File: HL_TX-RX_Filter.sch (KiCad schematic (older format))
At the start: 201 parts, among them J1 CNR1, J10 To Rx in, J2 CNR3, J3 Antenna, J4 CNR2, J5 CNR4, J6 From Tx, J7 ICSP, J8 SCL SDA, J9 Input1, Q1 2N7002, Q2 2N7002, Q3 2N7002, Q4 2N7002, Q5 2N7002, Q6 2N7002, Q7 2N7002, Q8 2N7002, U1 ATMEGA328-AU, U10 PE4259, U11 PE4259, U12 PE4259, U2 PE4259, U3 PE4259, U4 PE4259, U5 PE4259, U6 PE4259, U7 PE4259, U8 PE4259, U9 PE4259

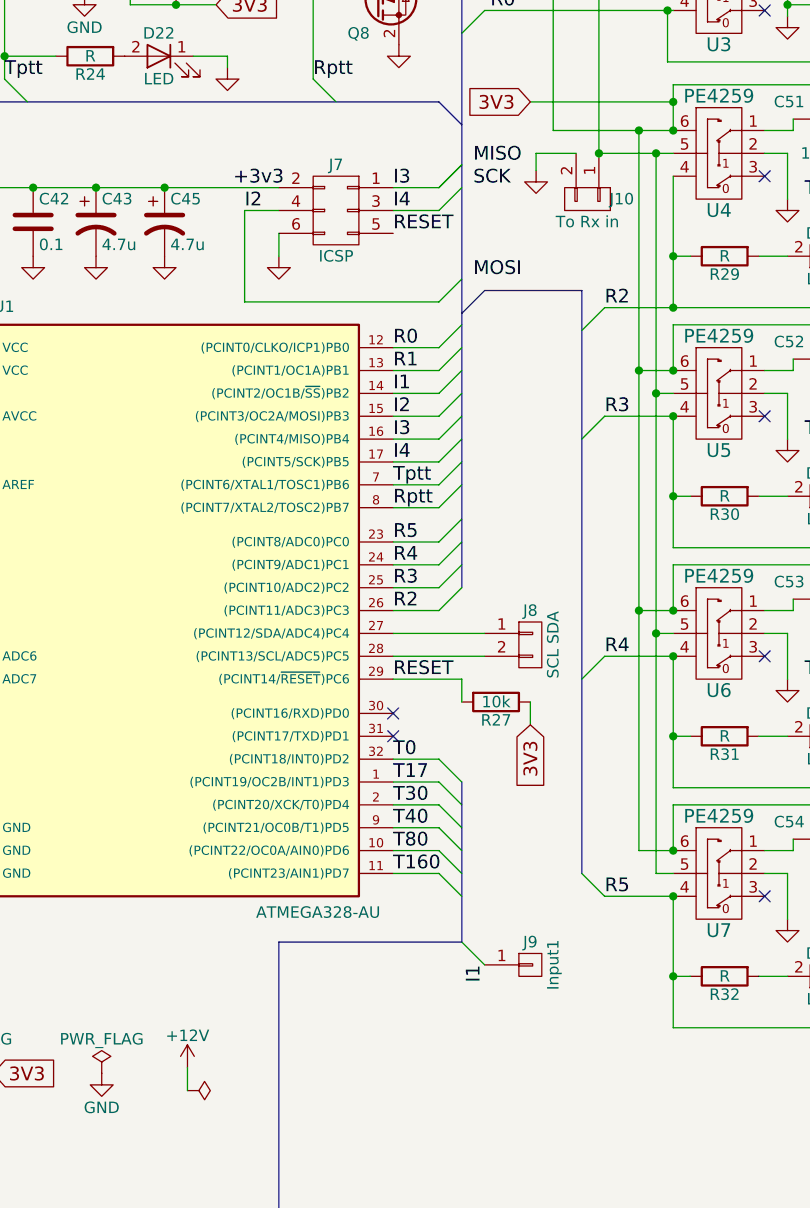
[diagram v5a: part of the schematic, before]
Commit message: Further progress on Filter switching lines
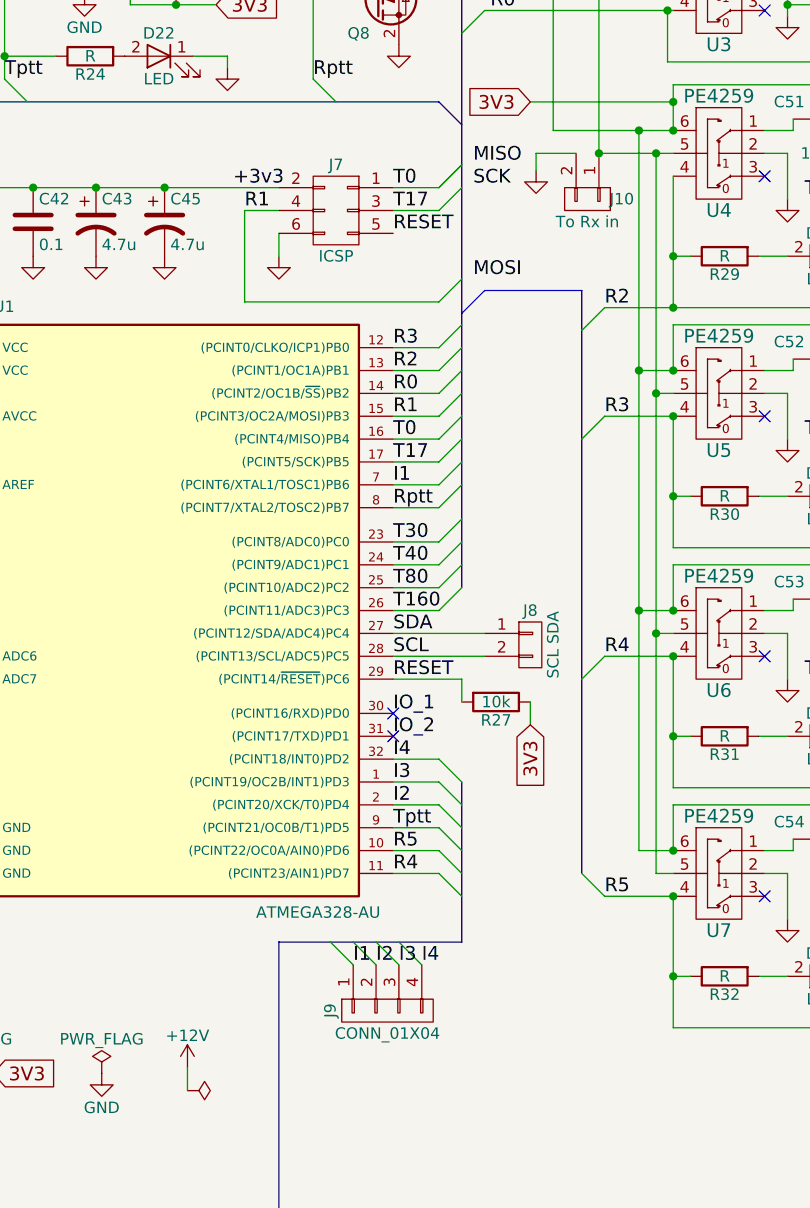
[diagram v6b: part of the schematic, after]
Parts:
- removed J9: Input1, Pin_Headers:Pin_Header_Straight_1x01_Pitch2.54mm, symbol CONN_01X01
- added J9: CONN_01X04, Pin_Headers:Pin_Header_Straight_1x04_Pitch2.54mm, symbol CONN_01X04
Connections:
- net I1: now also U1.7 ((PCINT6/XTAL1/TOSC1)PB6), J9.1 (P1); no longer U1.14 ((PCINT2/OC1B/~SS~)PB2)
- net I2: now also U1.2 ((PCINT20/XCK/T0)PD4), J9.2 (P2); no longer J7.4 (P4), U1.15 ((PCINT3/OC2A/MOSI)PB3)
- net I3: now also U1.1 ((PCINT19/OC2B/INT1)PD3), J9.3 (P3); no longer J7.1 (P1), U1.16 ((PCINT4/MISO)PB4)
- net I4: now also U1.32 ((PCINT18/INT0)PD2), J9.4 (P4); no longer J7.3 (P3), U1.17 ((PCINT5/SCK)PB5)
- net R0: now also U1.14 ((PCINT2/OC1B/~SS~)PB2); no longer U1.12 ((PCINT0/CLKO/ICP1)PB0)
- net R1: now also J7.4 (P4), U1.15 ((PCINT3/OC2A/MOSI)PB3); no longer U1.13 ((PCINT1/OC1A)PB1)
- net R2: now also U1.13 ((PCINT1/OC1A)PB1); no longer U1.26 ((PCINT11/ADC3)PC3)
- net R3: now also U1.12 ((PCINT0/CLKO/ICP1)PB0); no longer U1.25 ((PCINT10/ADC2)PC2)
- net R4: now also U1.11 ((PCINT23/AIN1)PD7); no longer U1.24 ((PCINT9/ADC1)PC1)
- net R5: now also U1.10 ((PCINT22/OC0A/AIN0)PD6); no longer U1.23 ((PCINT8/ADC0)PC0)
- net T0: now also J7.1 (P1), U1.16 ((PCINT4/MISO)PB4); no longer U1.32 ((PCINT18/INT0)PD2)
- net T160: now also U1.26 ((PCINT11/ADC3)PC3); no longer U1.11 ((PCINT23/AIN1)PD7)
- net T17: now also J7.3 (P3), U1.17 ((PCINT5/SCK)PB5); no longer U1.1 ((PCINT19/OC2B/INT1)PD3)
- net T30: now also U1.23 ((PCINT8/ADC0)PC0); no longer U1.2 ((PCINT20/XCK/T0)PD4)
- net T40: now also U1.24 ((PCINT9/ADC1)PC1); no longer U1.9 ((PCINT21/OC0B/T1)PD5)
- net T80: now also U1.25 ((PCINT10/ADC2)PC2); no longer U1.10 ((PCINT22/OC0A/AIN0)PD6)
- net Tptt: now also U1.9 ((PCINT21/OC0B/T1)PD5); no longer U1.7 ((PCINT6/XTAL1/TOSC1)PB6)
- net SDA: now reaches J8.1 (P1), U1.27 ((PCINT12/SDA/ADC4)PC4)
- net SCL: now reaches J8.2 (P2), U1.28 ((PCINT13/SCL/ADC5)PC5)
- net IO_1: now reaches U1.30 ((PCINT16/RXD)PD0)
- net IO_2: now reaches U1.31 ((PCINT17/TXD)PD1)
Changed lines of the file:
@@
 	7500 6050 7600 6150
 Text Label 7300 5550 0    60   ~ 0
-T0
+I4
 Text Label 7300 5650 0    60   ~ 0
-T17
+I3
 Text Label 7300 5750 0    60   ~ 0
-T30
+I2
 Text Label 7300 5850 0    60   ~ 0
-T40
+Tptt
 Text Label 7300 5950 0    60   ~ 0
-T80
+R5
 Text Label 7300 6050 0    60   ~ 0
-T160
+R4
 $Comp
 L R R25
@@
 	7500 4050 7600 3950
 Text Label 7300 3750 0    60   ~ 0
+R3
+Text Label 7300 3850 0    60   ~ 0
+R2
+Text Label 7300 3950 0    60   ~ 0
 R0
-Text Label 7300 3850 0    60   ~ 0
-R1
-Text Label 7300 3950 0    60   ~ 0
-I1
 Text Label 7300 4800 0    60   ~ 0
-R3
+T80
 Text Label 7300 4150 0    60   ~ 0
-I3
+T0
 Text Label 7300 4250 0    60   ~ 0
-I4
+T17
 Entry Wire Line
 	7600 2375 7700 2275
@@
 	7500 3150 7600 3050
 Text Label 7300 3050 0    60   ~ 0
-I3
+T0
 Text Label 7300 3150 0    60   ~ 0
-I4
+T17
 Text Label 7650 2950 0    60   ~ 0
 MISO
@@
 	7500 3550 7600 3450
 Text Label 6650 3150 0    60   ~ 0
-I2
+R1
 $Comp
 L GND #PWR054
@@
 	7500 4450 7600 4350
 Text Label 7300 4350 0    60   ~ 0
-Tptt
+I1
 Text Label 7300 4450 0    60   ~ 0
 Rptt
@@
 	7500 4600 7600 4500
 Text Label 7300 4600 0    60   ~ 0
-R5
+T30
 Text Label 7300 4700 0    60   ~ 0
-R4
+T40
 Text Label 7300 4050 0    60   ~ 0
-I2
+R1
 Text Label 7300 4900 0    60   ~ 0
-R2
-$Comp
-L CONN_01X01 J9
-U 1 1 59718308
-P 7900 6450
-F 0 "J9" H 7900 6550 50  0000 C CNN
-F 1 "Input1" V 8000 6450 50  0000 C CNN
-F 2 "Pin_Headers:Pin_Header_Straight_1x01_Pitch2.54mm" H 7900 6450 50  0001 C CNN
-F 3 "" H 7900 6450 50  0001 C CNN
-	1    7900 6450
-	1    0    0    -1
-$EndComp
-Entry Wire Line
-	7600 6350 7700 6450
-Text Label 7700 6450 3    60   ~ 0
+T160
+Entry Wire Line
+	7025 6350 7125 6450
+Text Label 7125 6450 0    60   ~ 0
 I1
 $Comp
@@
 	4550 1125 4550 6625
 Connection ~ 4550 1125
+Text Label 7300 5000 0    60   ~ 0
+SDA
+Text Label 7300 5100 0    60   ~ 0
+SCL
+Text Label 7300 5350 0    60   ~ 0
+IO_1
+Text Label 7300 5450 0    60   ~ 0
+IO_2
+$Comp
+L CONN_01X04 J9
+U 1 1 5975A6E8
+P 7275 6650
+F 0 "J9" H 7275 6900 50  0000 C CNN
+F 1 "CONN_01X04" V 7375 6650 50  0000 C CNN
+F 2 "Pin_Headers:Pin_Header_Straight_1x04_Pitch2.54mm" H 7275 6650 50  0001 C CNN
+F 3 "" H 7275 6650 50  0001 C CNN
+	1    7275 6650
+	0    -1   1    0
+$EndComp
+Text Label 7225 6450 0    60   ~ 0
+I2
+Text Label 7325 6450 0    60   ~ 0
+I3
+Text Label 7425 6450 0    60   ~ 0
+I4
+Entry Wire Line
+	7125 6350 7225 6450
+Entry Wire Line
+	7225 6350 7325 6450
+Entry Wire Line
+	7325 6350 7425 6450
 $EndSCHEMATC

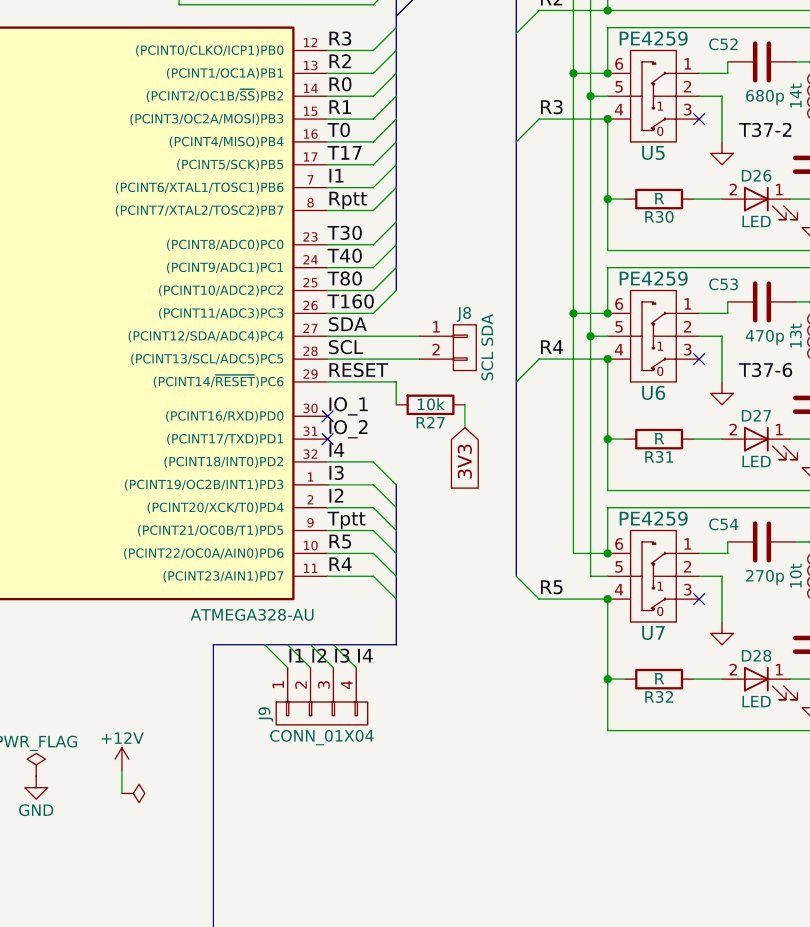
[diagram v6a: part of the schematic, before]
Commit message: Placing inputs to microprocessor
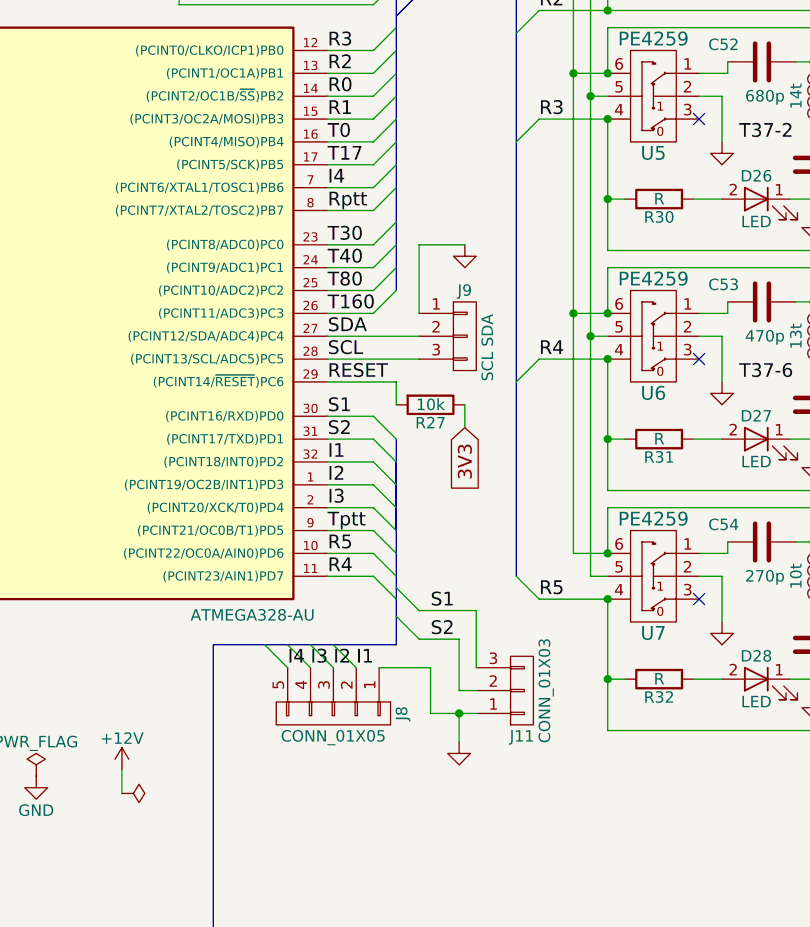
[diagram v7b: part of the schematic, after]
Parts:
- removed J8: SCL SDA, Pin_Headers:Pin_Header_Straight_1x02_Pitch2.54mm, symbol CONN_01X02
- removed J9: CONN_01X04, Pin_Headers:Pin_Header_Straight_1x04_Pitch2.54mm, symbol CONN_01X04
- added J11: CONN_01X03, Pin_Headers:Pin_Header_Straight_1x03_Pitch2.54mm, symbol CONN_01X03
- added J8: CONN_01X05, Pin_Headers:Pin_Header_Straight_1x05_Pitch2.54mm, symbol CONN_01X05
- added J9: SCL SDA, Pin_Headers:Pin_Header_Straight_1x03_Pitch2.54mm, symbol CONN_01X03
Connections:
- net GND: now also J11.1 (P1), J8.1 (P1), J9.1 (P1)
- net I1: now also U1.32 ((PCINT18/INT0)PD2), J8.2 (P2); no longer U1.7 ((PCINT6/XTAL1/TOSC1)PB6)
- net I2: now also U1.1 ((PCINT19/OC2B/INT1)PD3), J8.3 (P3); no longer U1.2 ((PCINT20/XCK/T0)PD4)
- net I3: now also U1.2 ((PCINT20/XCK/T0)PD4), J8.4 (P4); no longer U1.1 ((PCINT19/OC2B/INT1)PD3)
- net I4: now also U1.7 ((PCINT6/XTAL1/TOSC1)PB6), J8.5 (P5); no longer U1.32 ((PCINT18/INT0)PD2)
- net SCL: now also J9.3 (P3)
- net SDA: now also J9.2 (P2)
- net IO_1 renamed S1
- net S1: now also J11.3 (P3)
- net IO_2 renamed S2
- net S2: now also J11.2 (P2)
- no-connect marks 15 -> 13
